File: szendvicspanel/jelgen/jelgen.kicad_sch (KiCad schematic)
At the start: 21 parts, among them J1 Conn_01x04_Pin, J10 Conn_01x03_Socket, J2 Conn_01x03_Socket, J3 Conn_01x03_Pin, J4 Conn_01x03_Socket, J5 Conn_01x03_Socket, J6 Conn_01x03_Socket, J7 Conn_01x03_Socket, J8 Conn_01x03_Socket, J9 Conn_01x03_Socket, U1 TL072, U2 TL072

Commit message: PCB sketch 1
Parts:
- removed J3: Conn_01x03_Pin, symbol Connector:Conn_01x03_Pin
- added TJ1, TJ2, TJ3: Conn_01x01_Pin, Connector_PinHeader_2.54mm:PinHeader_1x01_P2.54mm_Vertical, symbol Connector:Conn_01x01_Pin
- C1, C2: footprint (none) -> Capacitor_THT:C_Axial_L5.1mm_D3.1mm_P7.50mm_Horizontal
- OJ1: renamed from J2; footprint (none) -> Connector_PinSocket_2.54mm:PinSocket_1x03_P2.54mm_Vertical
- OJ2: renamed from J4; footprint (none) -> Connector_PinSocket_2.54mm:PinSocket_1x03_P2.54mm_Vertical
- OJ3: renamed from J5; footprint (none) -> Connector_PinSocket_2.54mm:PinSocket_1x03_P2.54mm_Vertical
- OJ4: renamed from J6; footprint (none) -> Connector_PinSocket_2.54mm:PinSocket_1x03_P2.54mm_Vertical
- OJ5: renamed from J7; footprint (none) -> Connector_PinSocket_2.54mm:PinSocket_1x03_P2.54mm_Vertical
- OJ6: renamed from J8; footprint (none) -> Connector_PinSocket_2.54mm:PinSocket_1x03_P2.54mm_Vertical
- OJ7: renamed from J9; footprint (none) -> Connector_PinSocket_2.54mm:PinSocket_1x03_P2.54mm_Vertical
- OJ8: renamed from J10; footprint (none) -> Connector_PinSocket_2.54mm:PinSocket_1x03_P2.54mm_Vertical
- R1, R2, R3, R4: footprint (none) -> Resistor_THT:R_Axial_DIN0204_L3.6mm_D1.6mm_P5.08mm_Horizontal
- RV1, RV2, RV3: footprint (none) -> Potentiometer_THT:Potentiometer_Bourns_3266Y_Vertical
- U1, U2: footprint (none) -> Package_DIP:DIP-8_W7.62mm
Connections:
- net PWM: now also OJ1.1 (Pin_1), OJ2.1 (Pin_1), OJ3.1 (Pin_1), OJ4.1 (Pin_1), OJ5.1 (Pin_1), OJ6.1 (Pin_1), OJ7.1 (Pin_1), OJ8.1 (Pin_1), TJ3.1 (Pin_1); no longer OJ1.2 (Pin_2), OJ2.2 (Pin_2), OJ3.2 (Pin_2), OJ4.2 (Pin_2), OJ5.2 (Pin_2), OJ6.2 (Pin_2), OJ7.2 (Pin_2), OJ8.2 (Pin_2)
- net SQUARE: now also TJ1.1 (Pin_1)
- net TRIANGLE: now also TJ2.1 (Pin_1)
- net VPWR: now also OJ1.2 (Pin_2), OJ2.2 (Pin_2), OJ3.2 (Pin_2), OJ4.2 (Pin_2), OJ5.2 (Pin_2), OJ6.2 (Pin_2), OJ7.2 (Pin_2), OJ8.2 (Pin_2); no longer OJ1.1 (Pin_1), OJ2.1 (Pin_1), OJ3.1 (Pin_1), OJ4.1 (Pin_1), OJ5.1 (Pin_1), OJ6.1 (Pin_1), OJ7.1 (Pin_1), OJ8.1 (Pin_1)

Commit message: PCB sketch 2
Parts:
- removed TJ1, TJ2, TJ3: Conn_01x01_Pin, Connector_PinHeader_2.54mm:PinHeader_1x01_P2.54mm_Vertical, symbol Connector:Conn_01x01_Pin
- added TP1, TP2, TP3, TP4: TestPoint, Connector_PinHeader_2.54mm:PinHeader_1x01_P2.54mm_Vertical, symbol Connector:TestPoint
- J1: footprint Connector_PinHeader_2.54mm:PinHeader_1x04_P2.54mm_Horizontal -> Connector_PinHeader_2.54mm:PinHeader_1x04_P2.54mm_Vertical
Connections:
- net GND: now also OJ1.1 (Pin_1), OJ2.1 (Pin_1), OJ3.1 (Pin_1), OJ4.1 (Pin_1), OJ5.1 (Pin_1), OJ6.1 (Pin_1), OJ7.1 (Pin_1), OJ8.1 (Pin_1); no longer OJ1.3 (Pin_3), OJ2.3 (Pin_3), OJ3.3 (Pin_3), OJ4.3 (Pin_3), OJ5.3 (Pin_3), OJ6.3 (Pin_3), OJ7.3 (Pin_3), OJ8.3 (Pin_3)
- net REF: now also TP4.1
- net SQUARE: now also TP1.1
- net TRIANGLE: now also TP2.1
- removed net PWM: OJ1.1 (Pin_1), OJ2.1 (Pin_1), OJ3.1 (Pin_1), OJ4.1 (Pin_1), OJ5.1 (Pin_1), OJ6.1 (Pin_1), OJ7.1 (Pin_1), OJ8.1 (Pin_1), U2.7
- new net OUT_ARRAY_PIN3: OJ1.3 (Pin_3), OJ2.3 (Pin_3), OJ3.3 (Pin_3), OJ4.3 (Pin_3), OJ5.3 (Pin_3), OJ6.3 (Pin_3), OJ7.3 (Pin_3), OJ8.3 (Pin_3), TP3.1, U2.7
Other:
- moved on the sheet: OJ1, OJ2, OJ3, OJ4, OJ5, OJ6, OJ7, OJ8

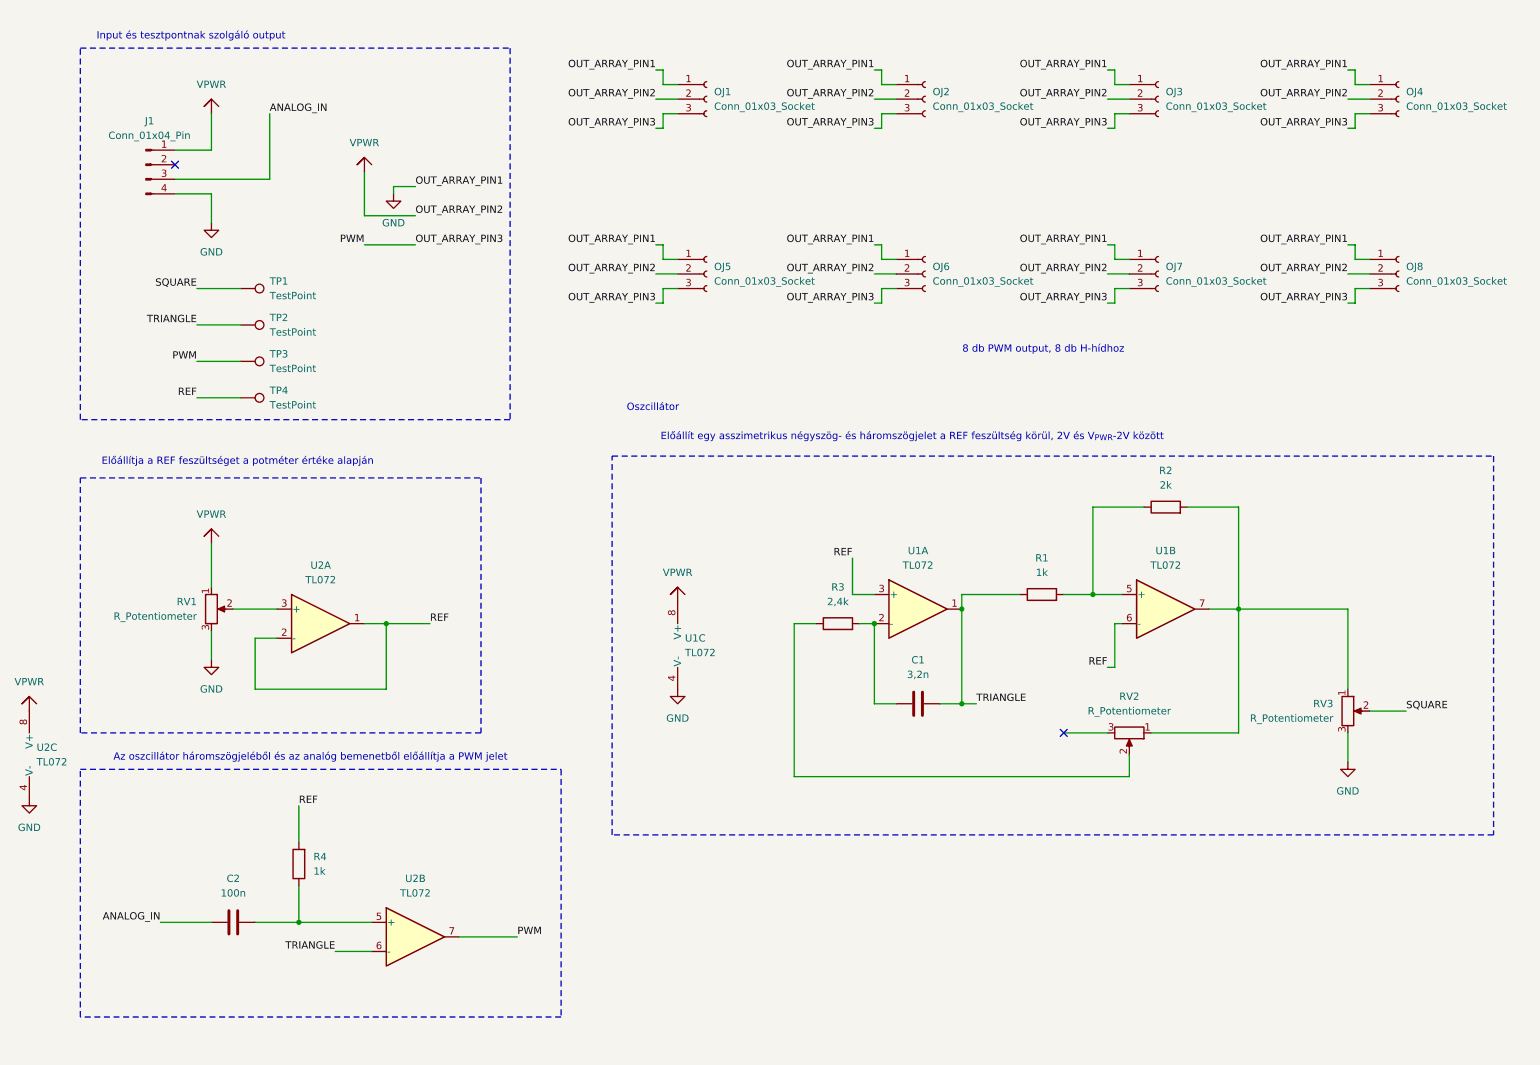
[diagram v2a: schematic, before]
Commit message: Ground plane, output array áttervezés, input horizontal footprint
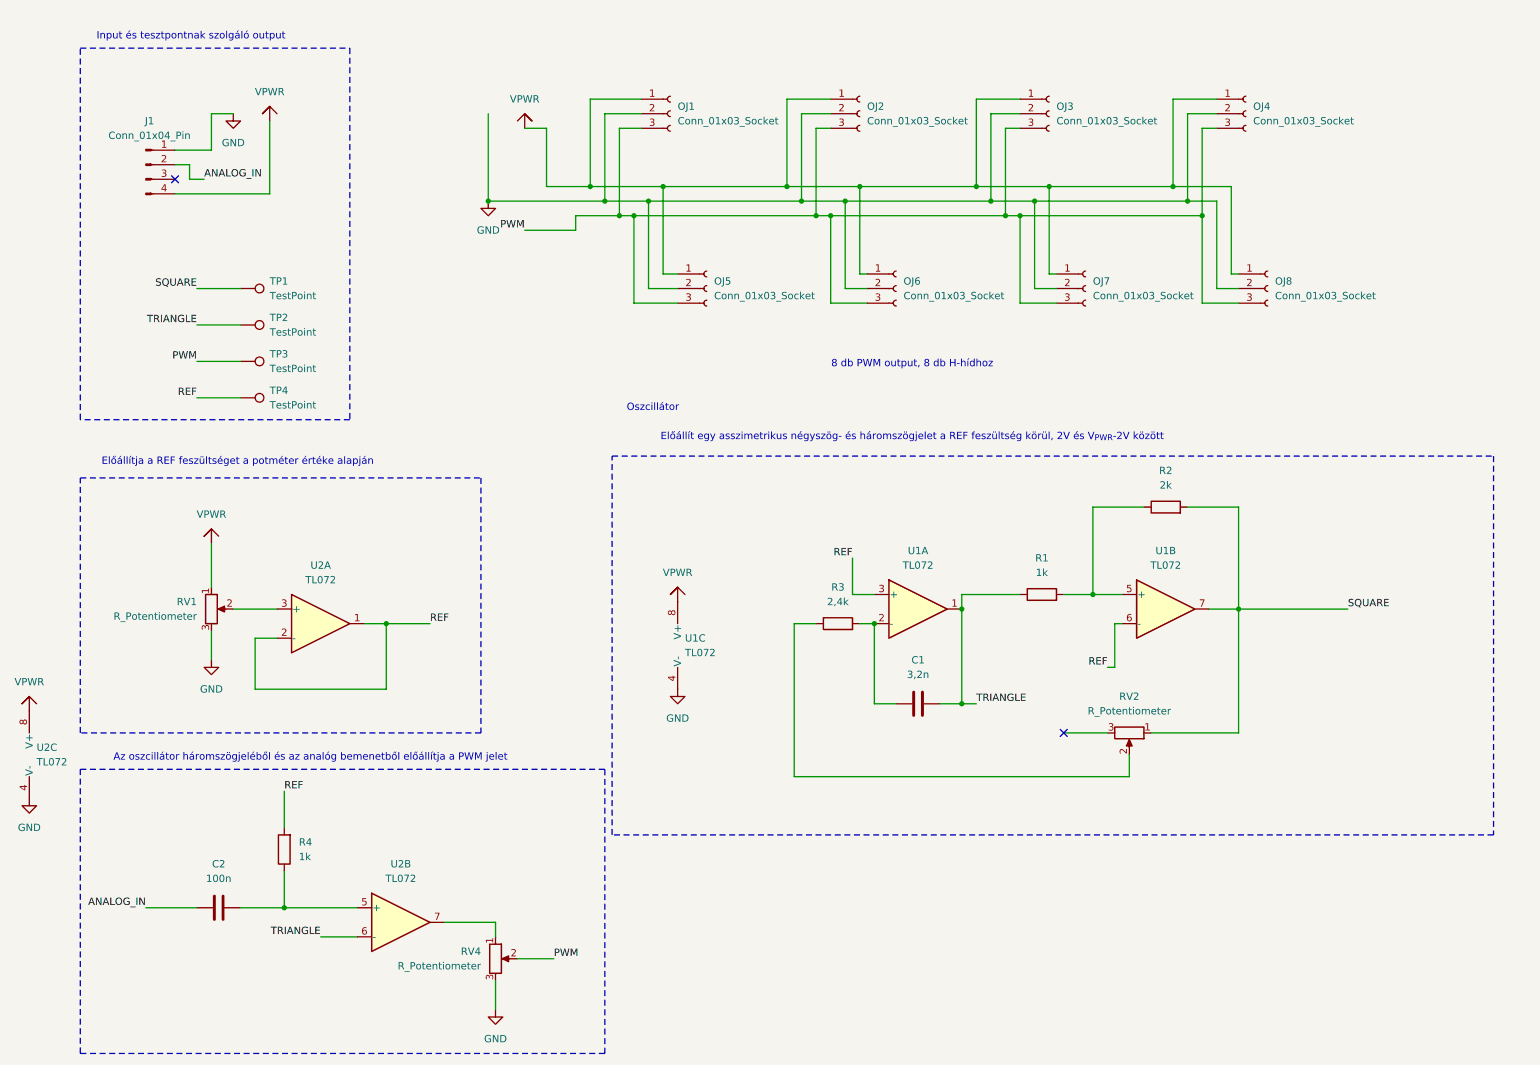
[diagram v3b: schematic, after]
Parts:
- removed RV3: R_Potentiometer, Potentiometer_THT:Potentiometer_Bourns_3266Y_Vertical, symbol Device:R_Potentiometer
- added RV4: R_Potentiometer, Potentiometer_THT:Potentiometer_Bourns_3266Y_Vertical, symbol Device:R_Potentiometer
- J1: footprint Connector_PinHeader_2.54mm:PinHeader_1x04_P2.54mm_Vertical -> Connector_PinHeader_2.54mm:PinHeader_1x04_P2.54mm_Horizontal
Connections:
- net ANALOG_IN: now also J1.2 (Pin_2); no longer J1.3 (Pin_3)
- net GND: now also J1.1 (Pin_1), OJ1.2 (Pin_2), OJ2.2 (Pin_2), OJ3.2 (Pin_2), OJ4.2 (Pin_2), OJ5.2 (Pin_2), OJ6.2 (Pin_2), OJ7.2 (Pin_2), OJ8.2 (Pin_2), RV4.3; no longer J1.4 (Pin_4), OJ1.1 (Pin_1), OJ2.1 (Pin_1), OJ3.1 (Pin_1), OJ4.1 (Pin_1), OJ5.1 (Pin_1), OJ6.1 (Pin_1), OJ7.1 (Pin_1), OJ8.1 (Pin_1)
- net SQUARE: now also R2.2, RV2.1, U1.7
- net VPWR: now also J1.4 (Pin_4), OJ1.1 (Pin_1), OJ2.1 (Pin_1), OJ3.1 (Pin_1), OJ4.1 (Pin_1), OJ5.1 (Pin_1), OJ6.1 (Pin_1), OJ7.1 (Pin_1), OJ8.1 (Pin_1); no longer J1.1 (Pin_1), OJ1.2 (Pin_2), OJ2.2 (Pin_2), OJ3.2 (Pin_2), OJ4.2 (Pin_2), OJ5.2 (Pin_2), OJ6.2 (Pin_2), OJ7.2 (Pin_2), OJ8.2 (Pin_2)
- net OUT_ARRAY_PIN3 renamed PWM
- net PWM: now also RV4.2; no longer U2.7
- new net: RV4.1, U2.7
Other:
- moved on the sheet: C2, OJ1, OJ2, OJ3, OJ4, OJ5, OJ6, OJ7, OJ8, R4, U2B
